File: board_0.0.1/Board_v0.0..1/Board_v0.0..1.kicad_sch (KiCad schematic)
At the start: 1 part, among them U1 Teensy3.5

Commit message: iginition & fuel
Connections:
- net GND: now reaches U1.1 (GND)
- net GND: now also U1.27 (GND), U1.61 (GND), U1.62 (GND)
- net VBat: now reaches U1.25 (VBat)
- net +3V3: now reaches U1.26 (3.3V)
- net PROG: now reaches U1.28 (Program)
- net RESET: now reaches U1.29 (Reset)

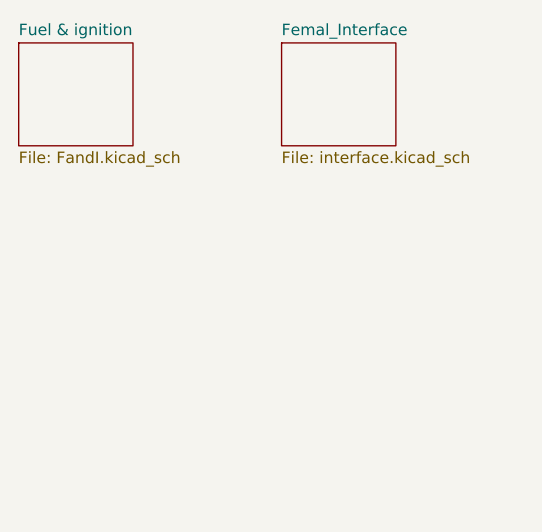
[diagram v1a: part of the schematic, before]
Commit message: added sensor page and basic wiring, hope to find some pepole to help me wis some sensot wiring
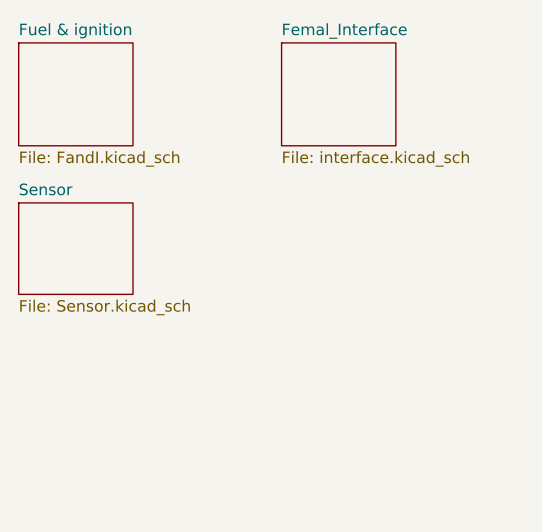
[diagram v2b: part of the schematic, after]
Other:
- added sheet Sensor (Sensor.kicad_sch)
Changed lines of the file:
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@@
+	)
+	(sheet
+		(at 27.94 41.91)
+		(size 12.7 10.16)
+		(fields_autoplaced yes)
+		(stroke
+			(width 0.1524)
+			(type solid)
+		)
+		(fill
+			(color 0 0 0 0.0000)
+		)
+		(property "Sheetname" "Sensor"
+			(at 27.94 41.1984 0)
+			(effects
+				(font
+					(size 1.27 1.27)
+				)
+				(justify left bottom)
+			)
+		)
+		(property "Sheetfile" "Sensor.kicad_sch"
+			(at 27.94 52.6546 0)
+			(effects
+				(font
+					(size 1.27 1.27)
+				)
+				(justify left top)
+			)
+		)
+		(instances
+			(project "Board_v0.0..1"
+				(path "/84a654bf-6339-4456-82e8-fc3535e299fc"
+					(page "5")
+				)
+			)
+		)
 	)
 	(sheet
